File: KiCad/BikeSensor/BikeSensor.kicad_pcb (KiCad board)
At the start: 2 copper layers, 15 x 33 mm, 37 parts, among them J1 USB_C_Receptacle_TYPE-C 16PIN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, SW2 SW_MEC_5G, U1 MDBT50Q-1MV2, U11 TPD4E02B04DQA, U2 LSM6DSV, U6 BAT, U7 MCP73831-2-MC, U9 TPS7A0233DQNR, X1 32.768KHz

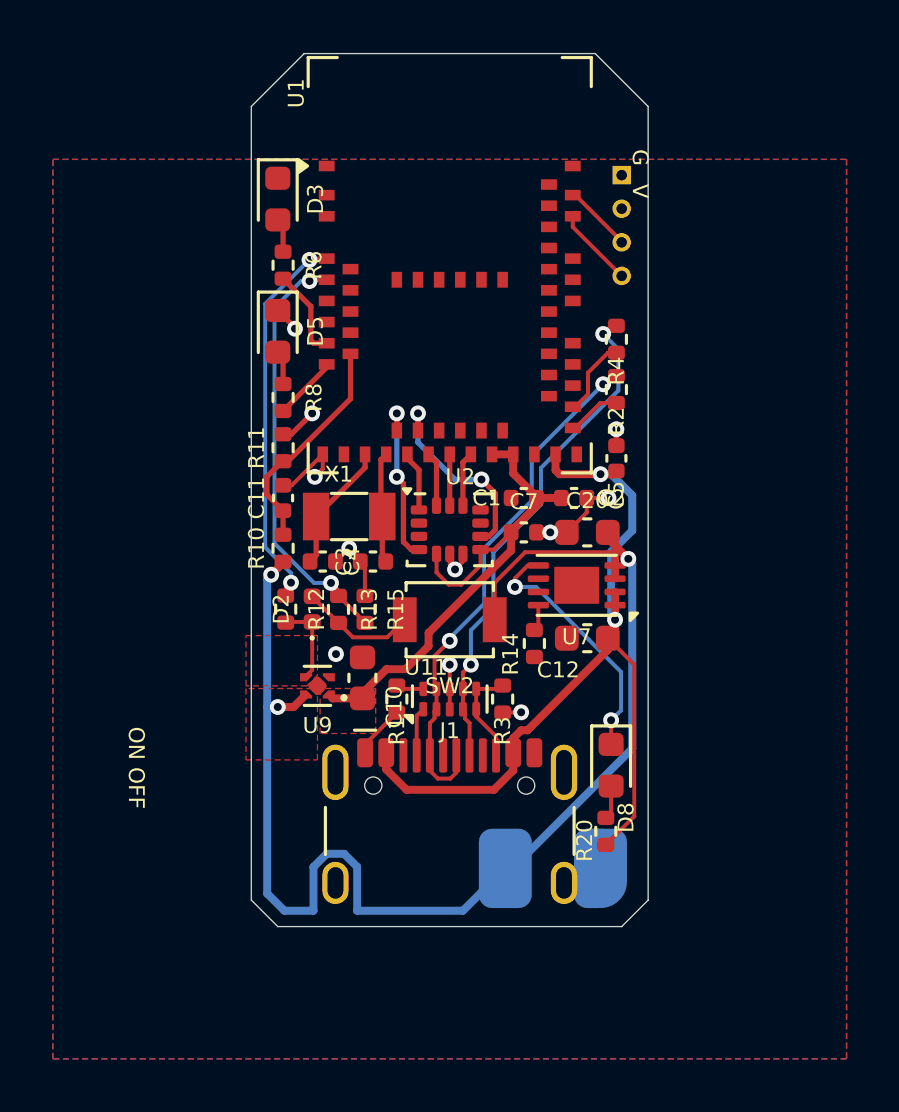
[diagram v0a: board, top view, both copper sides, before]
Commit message: add: BikeSensor PCB v1 (renamed from RideFormTracker) and the 320X datasheet
The KiCad project is renamed to match what it actually became: not a
RideFormTracker variant but its own 15x33 mm board, with a soft power
latch, BAT_CHECK moved to an analog-capable pin, and an LSM6DSV320X.

Also carries the production files as sent to the fab. Those are
regenerable in principle, but the first article had an open PROG trace -
the charger sat in its shutdown state and neither charged nor lit its
status LED - and being able to compare a board in hand against exactly
what was ordered is worth the few hundred kilobytes.
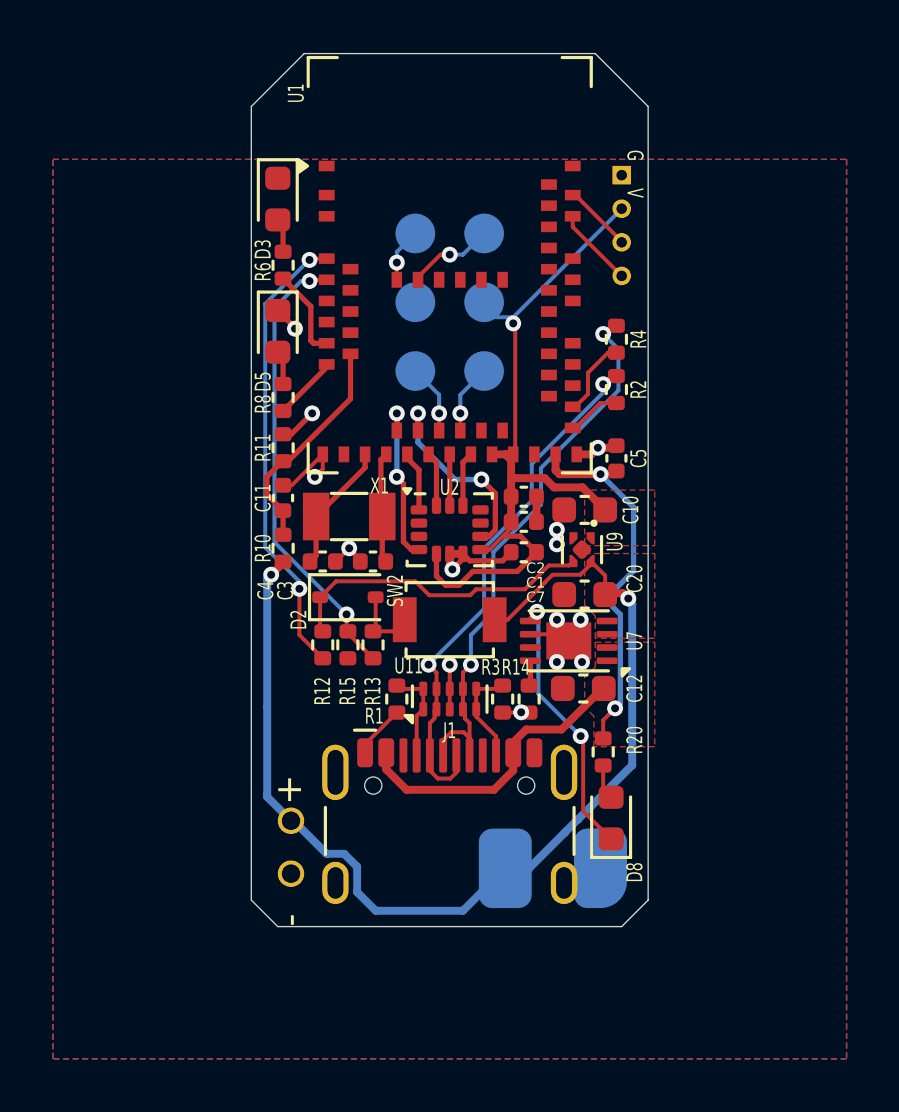
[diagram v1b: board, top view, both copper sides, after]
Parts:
- added H1: ~, ThroughHole:TH_0.7mm, F.Cu at (94.0, 106.0)
- added H2: ~, ThroughHole:TH_0.7mm, F.Cu at (94.0, 108.0)
- added TP1: TestPoint, TestPoint:TestPoint_Pad_D1.5mm, B.Cu at (98.7, 89.0)
- added TP2: TestPoint, TestPoint:TestPoint_Pad_D1.5mm, B.Cu at (101.3, 89.0)
- added TP3: TestPoint, TestPoint:TestPoint_Pad_D1.5mm, B.Cu at (98.7, 83.8)
- added TP4: TestPoint, TestPoint:TestPoint_Pad_D1.5mm, B.Cu at (101.3, 83.8)
- added TP5: TestPoint, TestPoint:TestPoint_Pad_D1.5mm, B.Cu at (101.3, 86.4)
- added TP6: TestPoint, TestPoint:TestPoint_Pad_D1.5mm, B.Cu at (98.7, 86.4)
- D2: footprint Diode_SMD:D_0402_1005Metric -> Diode_SMD:D_SOD-323
- U2: value LSM6DSV -> LSM6DSV320XTR
- U9: value TPS7A0233DQNR -> TPS7A0233PDQNR
- moved U9 11.2 mm to (105.0, 95.8), turned to -90 degrees
- moved C10 10.5 mm to (105.1, 94.2), turned to 180 degrees
- moved R20 3.00 mm to (105.8, 103.4), turned to 90 degrees
- moved C20 2.35 mm to (105.1, 97.5)
- moved U7 2.12 mm to (104.5, 99.2)
- moved R14 2.11 mm to (103.0, 101.4)
- moved D8 2.00 mm to (106.1, 105.9), turned to 90 degrees
- moved R12 1.94 mm to (95.2, 99.3), turned to 90 degrees
- moved C12 1.91 mm to (105.0, 101.0)
- moved C2 1.90 mm to (102.8, 93.8)
- moved R13 1.87 mm to (97.1, 99.3), turned to 90 degrees
- moved R15 1.49 mm to (96.2, 99.3), turned to 90 degrees
- moved D2 1.42 mm to (96.2, 97.5), turned to 0 degrees
- moved C1 0.90 mm to (102.8, 94.7), turned to 0 degrees
- moved C7 0.75 mm to (102.8, 95.8), turned to 180 degrees
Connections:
- U1 pad 23: unconnected-(U1-P0.07-Pad23) -> Net-(U1-P0.07)
- U1 pad 25: unconnected-(U1-P1.08-Pad25) -> Net-(U1-P1.08)
- U1 pad 56: unconnected-(U1-P1.04-Pad56) -> Net-(U1-P1.04)
- U1 pad 57: unconnected-(U1-P1.06-Pad57) -> Net-(U1-P1.06)
- U5 pad 1: +V_BAT -> +3.3V
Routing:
- net +V_BAT: track 51.6 -> 41.1 mm, vias 3 -> 2
- net LDO_EN: track 3.18 -> 11.9 mm
- net +3.3V: track 20.6 -> 28.4 mm, vias 0 -> 1
- net +5V: track 32.9 -> 25.6 mm
- net Net-(U1-P1.06): track 0.00 -> 3.28 mm, vias 0 -> 1
- net SOFT_LATCH: track 14.5 -> 17.3 mm
- net Net-(U1-P1.08): track 0.00 -> 2.62 mm, vias 0 -> 1
- net Net-(U1-P0.07): track 0.00 -> 2.62 mm, vias 0 -> 1
- net Net-(U11-IO3): track 19.3 -> 21.8 mm
- net Net-(U1-P1.04): track 0.00 -> 2.04 mm, vias 0 -> 1
- net Net-(D2-A): track 4.42 -> 2.71 mm
- net SW_READ: track 16.1 -> 17.2 mm
- net GND_POWER: track 19.2 -> 20.2 mm, vias 11 -> 14
- net Net-(J1-CC1): track 2.90 -> 3.67 mm
- net Net-(D8-K): track 9.65 -> 10.2 mm
- added copper zone on F.Cu, net +5V
- removed copper zone on F.Cu, net LDO_EN
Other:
- board text removed: "BikeSensor"
- board text removed: "ON OFF"

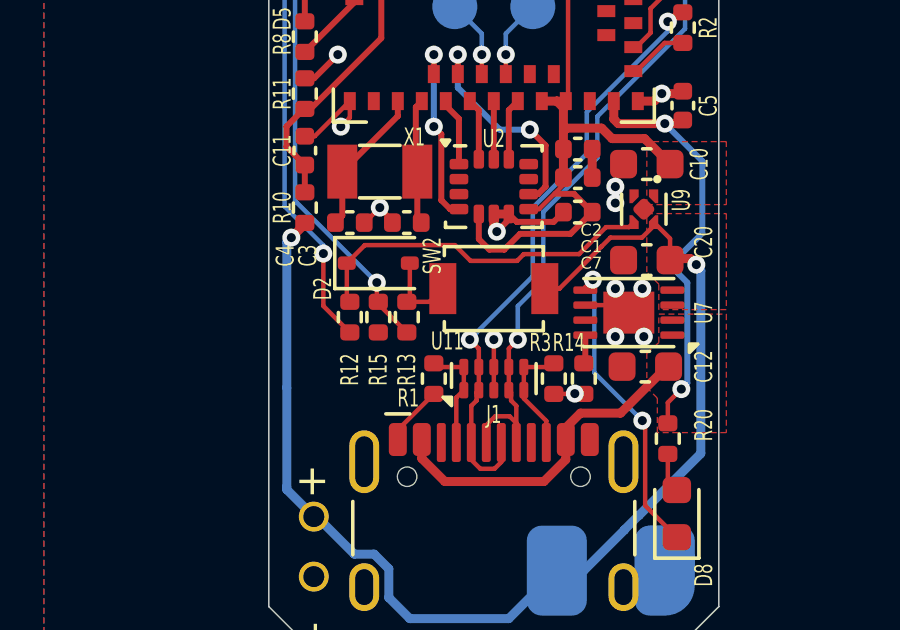
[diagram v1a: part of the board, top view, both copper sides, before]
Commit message: add: soft-latch rework, 10M battery divider and a 3D-printed case
Three changes to the enable network, none of which the firmware notices -
the pin assignments are identical, so one image runs on both revisions.

R13 moves to sit in series with SW2. The existing SW_READ divider then
also drops the voltage that reaches LDO_EN, which lands the button path
at 2.97 V instead of 3.95 V. That matters because R12 ties the enable
node straight to P1.11: the old level sat just under the GPIO's ESD
diode and therefore just outside its absolute maximum of VDD + 0.3 V.
Costs nothing - the divider ratio, the SW_READ level and the 9.8 uA
drawn while the button is held are all unchanged.

VBUS reaches the enable node through a 100k/100k divider and D4, so
plugging in USB now starts the board. Previously the button was the only
way in, which was least convenient exactly when the pack was flat. After
a low-battery cutoff a cable now both charges and brings the board up.

With those two, every source that can raise the enable node stays at or
below VDD: 2.25 V from USB, 2.97 V from the button, 3.30 V from the GPIO.

The divider is not there for the LDO's sake - its EN pin is rated to
6.0 V and 5 V direct would be fine. It is there for the GPIO. Dropping
the voltage with a diode's Vf instead cannot work: Vf is a strong
function of current and at I_EN = 10 nA even silicon gives 0.2-0.3 V.
What sets the resistor values is not the ratio but the LDO's 500 kohm
smart enable pulldown, which is engaged at startup and swamps any
divider that is not stiff against it.

The GPIO branch deliberately keeps no diode of its own. Three diodes
would make a symmetric wired-OR, but the GPIO would lose the ability to
pull the enable node DOWN, and today's power-off is an active discharge
through R12 - a one-microsecond time constant that beats any plausible
leakage. Restoring that would need a pulldown, which shortens the
enable node's hold through a reset from ~2 ms to ~100 us and so needs a
capacitor a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
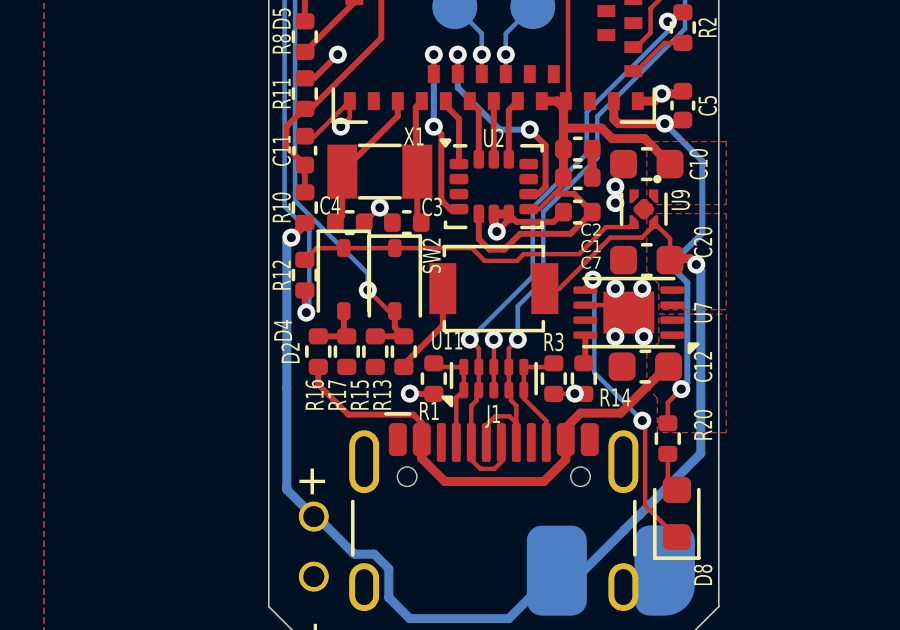
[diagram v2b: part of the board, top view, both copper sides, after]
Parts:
- added D4: D, Diode_SMD:D_SOD-323, F.Cu at (95.0, 98.1)
- added R16: 100k, Resistor_SMD:R_0402_1005Metric, F.Cu at (94.2, 100.5)
- added R17: 100k, Resistor_SMD:R_0402_1005Metric, F.Cu at (95.1, 100.5)
- R10, R11: value 1M -> 10M
- moved R12 2.05 mm to (93.7, 98.0)
- moved R15 1.15 mm to (96.0, 100.5), turned to -90 degrees
- moved R13 1.15 mm to (97.0, 100.5), turned to -90 degrees
- moved D2 0.78 mm to (96.7, 98.1), turned to -90 degrees
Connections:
- D2 pad 2: Net-(D2-A) -> SW_READ
- R13 pad 2: Net-(D2-A) -> Net-(R13-Pad2)
- R15 pad 1: GND_POWER -> SW_READ
- R15 pad 2: SW_READ -> GND_POWER
- SW2 pad 2: Net-(D2-A) -> Net-(R13-Pad2)
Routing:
- net +5V: track 25.6 -> 30.7 mm
- net Net-(R13-Pad2): track 0.00 -> 3.15 mm
- net Net-(D2-A): track 2.71 -> 0.00 mm
- net Net-(D4-A): track 0.00 -> 1.83 mm
- net SW_READ: track 17.2 -> 18.4 mm
- net GND_POWER: track 20.2 -> 19.3 mm, vias 14 -> 15
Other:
- board text added: "G"
- board text added: "V"
